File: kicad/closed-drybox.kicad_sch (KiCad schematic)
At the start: 25 parts, among them J1 Power_Jack, M1 Fan, M2 Fan, Q1 AO3400A, Q2 AO3400A, Q3 AO3400A, Q4 AO3400A, Q5 AO3400A, Q6 AO3400A, Q7 AO3400A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

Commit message: add anotations
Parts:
- gave numbers to parts that had none: 1
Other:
- moved on the sheet: JP1
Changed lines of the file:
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@@
 	(wire
 		(pts
-			(xy 120.65 46.99) (xy 124.46 46.99)
+			(xy 116.84 46.99) (xy 124.46 46.99)
 		)
 		(stroke
@@
 	(wire
 		(pts
-			(xy 113.03 46.99) (xy 55.88 46.99)
+			(xy 109.22 46.99) (xy 55.88 46.99)
 		)
 		(stroke
@@
 	(symbol
 		(lib_id "Jumper:SolderJumper_2_Open")
-		(at 116.84 46.99 0)
+		(at 113.03 46.99 0)
 		(unit 1)
 		(exclude_from_sim no)
@@
 		(dnp no)
 		(fields_autoplaced yes)
-		(property "Reference" "JP?"
-			(at 116.84 40.64 0)
+		(property "Reference" "JP1"
+			(at 113.03 40.64 0)
 			(effects
 				(font
@@
 		)
 		(property "Value" "SolderJumper_2_Open"
-			(at 116.84 43.18 0)
+			(at 113.03 43.18 0)
 			(effects
 				(font
@@
 		)
 		(property "Footprint" "Jumper:SolderJumper-2_P1.3mm_Open_RoundedPad1.0x1.5mm"
-			(at 116.84 46.99 0)
+			(at 113.03 46.99 0)
 			(effects
 				(font
@@
 		)
 		(property "Datasheet" "~"
-			(at 116.84 46.99 0)
+			(at 113.03 46.99 0)
 			(effects
 				(font
@@
 		)
 		(property "Description" "Solder Jumper, 2-pole, open"
-			(at 116.84 46.99 0)
+			(at 113.03 46.99 0)
 			(effects
 				(font
@@
 			(project ""
 				(path "/99399f2a-756c-4718-9b6a-bb37855e6538"
-					(reference "JP?")
+					(reference "JP1")
 					(unit 1)
 				)

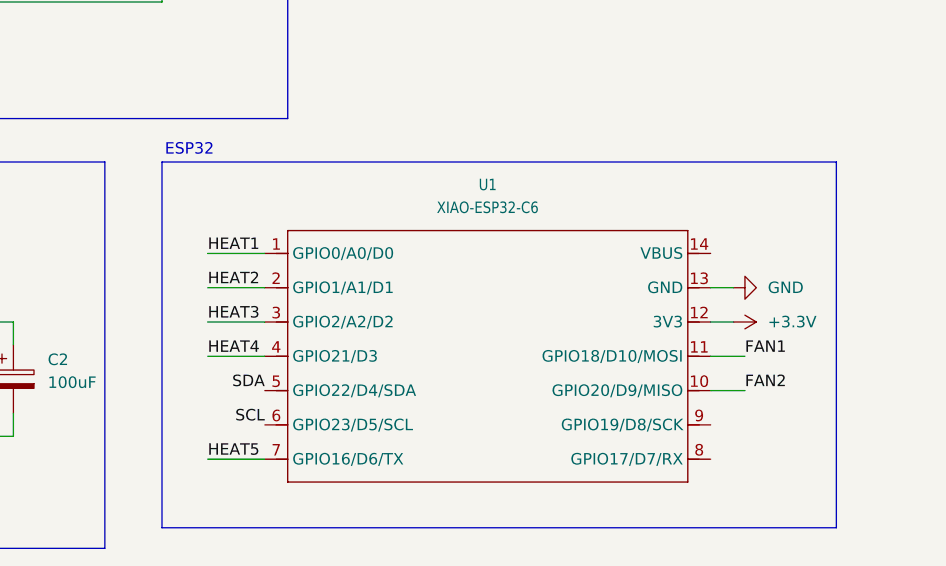
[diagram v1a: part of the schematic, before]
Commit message: fix labels
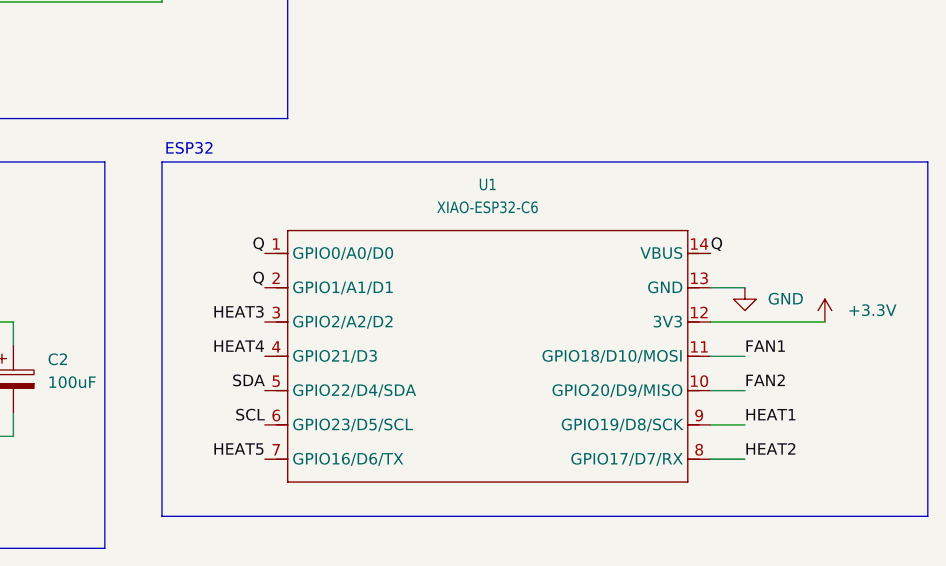
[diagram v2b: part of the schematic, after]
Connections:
- net HEAT1: now also U1.9 (GPIO19/D8/SCK); no longer U1.1 (GPIO0/A0/D0)
- net HEAT2: now also U1.8 (GPIO17/D7/RX); no longer U1.2 (GPIO1/A1/D1)
- net Q: now reaches U1.14 (VBUS)
- net Q: now also U1.1 (GPIO0/A0/D0), U1.2 (GPIO1/A1/D1)
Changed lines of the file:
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@@
 	(rectangle
 		(start 115.57 106.68)
-		(end 190.5 147.32)
+		(end 200.66 146.05)
 		(stroke
 			(width 0)
@@
 	(wire
 		(pts
-			(xy 176.53 120.65) (xy 179.07 120.65)
+			(xy 176.53 120.65) (xy 180.34 120.65)
 		)
 		(stroke
@@
 	(wire
 		(pts
-			(xy 120.65 116.84) (xy 127 116.84)
-		)
-		(stroke
-			(width 0)
-			(type default)
-		)
-	)
-	(wire
-		(pts
 			(xy 50.8 73.66) (xy 50.8 76.2)
 		)
@@
 	(wire
 		(pts
+			(xy 176.53 135.89) (xy 180.34 135.89)
+		)
+		(stroke
+			(width 0)
+			(type default)
+		)
+	)
+	(wire
+		(pts
 			(xy 109.22 46.99) (xy 55.88 46.99)
 		)
@@
 	(wire
 		(pts
-			(xy 176.53 124.46) (xy 179.07 124.46)
+			(xy 176.53 124.46) (xy 189.23 124.46)
 		)
 		(stroke
@@
 	(wire
 		(pts
-			(xy 120.65 120.65) (xy 127 120.65)
-		)
-		(stroke
-			(width 0)
-			(type default)
-		)
-	)
-	(wire
-		(pts
 			(xy 50.8 63.5) (xy 29.21 63.5)
 		)
@@
 	(wire
 		(pts
-			(xy 120.65 139.7) (xy 127 139.7)
-		)
-		(stroke
-			(width 0)
-			(type default)
-		)
-	)
-	(wire
-		(pts
 			(xy 72.39 86.36) (xy 72.39 88.9)
 		)
@@
 	(wire
 		(pts
-			(xy 120.65 124.46) (xy 127 124.46)
-		)
-		(stroke
-			(width 0)
-			(type default)
-		)
-	)
-	(wire
-		(pts
 			(xy 124.46 25.4) (xy 124.46 30.48)
 		)
@@
 	(wire
 		(pts
-			(xy 120.65 128.27) (xy 127 128.27)
-		)
-		(stroke
-			(width 0)
-			(type default)
-		)
-	)
-	(wire
-		(pts
 			(xy 176.53 34.29) (xy 176.53 27.94)
 		)
@@
 		(pts
 			(xy 99.06 124.46) (xy 83.82 124.46)
+		)
+		(stroke
+			(width 0)
+			(type default)
+		)
+	)
+	(wire
+		(pts
+			(xy 176.53 139.7) (xy 180.34 139.7)
 		)
 		(stroke
@@
 	)
 	(label "HEAT3"
-		(at 120.65 124.46 0)
+		(at 127 124.46 180)
+		(effects
+			(font
+				(size 1.27 1.27)
+			)
+			(justify right bottom)
+		)
+	)
+	(label "Q"
+		(at 176.53 116.84 0)
 		(effects
 			(font
@@
 		)
 	)
+	(label "Q"
+		(at 127 116.84 180)
+		(effects
+			(font
+				(size 1.27 1.27)
+			)
+			(justify right bottom)
+		)
+	)
 	(label "HEAT3"
 		(at 64.77 81.28 180)
@@
 		)
 	)
+	(label "Q"
+		(at 127 120.65 180)
+		(effects
+			(font
+				(size 1.27 1.27)
+			)
+			(justify right bottom)
+		)
+	)
 	(label "FAN1"
 		(at 143.51 55.88 180)
@@
 	)
 	(label "HEAT5"
-		(at 120.65 139.7 0)
+		(at 127 139.7 180)
 		(effects
 			(font
 				(size 1.27 1.27)
 			)
-			(justify left bottom)
+			(justify right bottom)
 		)
 	)
 	(label "HEAT1"
-		(at 120.65 116.84 0)
+		(at 180.34 135.89 0)
 		(effects
 			(font
@@
 	)
 	(label "HEAT2"
-		(at 120.65 120.65 0)
+		(at 180.34 139.7 0)
 		(effects
 			(font
@@
 	)
 	(label "HEAT4"
-		(at 120.65 128.27 0)
+		(at 127 128.27 180)
 		(effects
 			(font
 				(size 1.27 1.27)
 			)
-			(justify left bottom)
+			(justify right bottom)
 		)
 	)
@@
 	(symbol
 		(lib_id "power:+3.3V")
-		(at 179.07 124.46 270)
+		(at 189.23 124.46 0)
 		(unit 1)
 		(exclude_from_sim no)
@@
 		(fields_autoplaced yes)
 		(property "Reference" "#PWR08"
-			(at 175.26 124.46 0)
+			(at 189.23 128.27 0)
 			(effects
 				(font
@@
 		)
 		(property "Value" "+3.3V"
-			(at 182.88 124.4599 90)
+			(at 191.77 123.1899 0)
 			(effects
 				(font
@@
 		)
 		(property "Footprint" ""
-			(at 179.07 124.46 0)
+			(at 189.23 124.46 0)
 			(effects
 				(font
@@
 		)
 		(property "Datasheet" ""
-			(at 179.07 124.46 0)
+			(at 189.23 124.46 0)
 			(effects
 				(font
@@
 		)
 		(property "Description" "Power symbol creates a global label with name \"+3.3V\""
-			(at 179.07 124.46 0)
+			(at 189.23 124.46 0)
 			(effects
 				(font
@@
 	(symbol
 		(lib_id "power:GND")
-		(at 179.07 120.65 90)
+		(at 180.34 120.65 0)
 		(unit 1)
 		(exclude_from_sim no)
@@
 		(fields_autoplaced yes)
 		(property "Reference" "#PWR07"
-			(at 185.42 120.65 0)
+			(at 180.34 127 0)
 			(effects
 				(font
@@
 		)
 		(property "Value" "GND"
-			(at 182.88 120.6499 90)
-			(effects
-				(font
-					(size 1.27 1.27)
-				)
-				(justify right)
+			(at 182.88 121.9199 0)
+			(effects
+				(font
+					(size 1.27 1.27)
+				)
+				(justify left)
 			)
 		)
 		(property "Footprint" ""
-			(at 179.07 120.65 0)
+			(at 180.34 120.65 0)
 			(effects
 				(font
@@
 		)
 		(property "Datasheet" ""
-			(at 179.07 120.65 0)
+			(at 180.34 120.65 0)
 			(effects
 				(font
@@
 		)
 		(property "Description" "Power symbol creates a global label with name \"GND\" , ground"
-			(at 179.07 120.65 0)
-			(effects
-				(font
+			(at 180.34 120.65 0)
+			(effects
+				(font

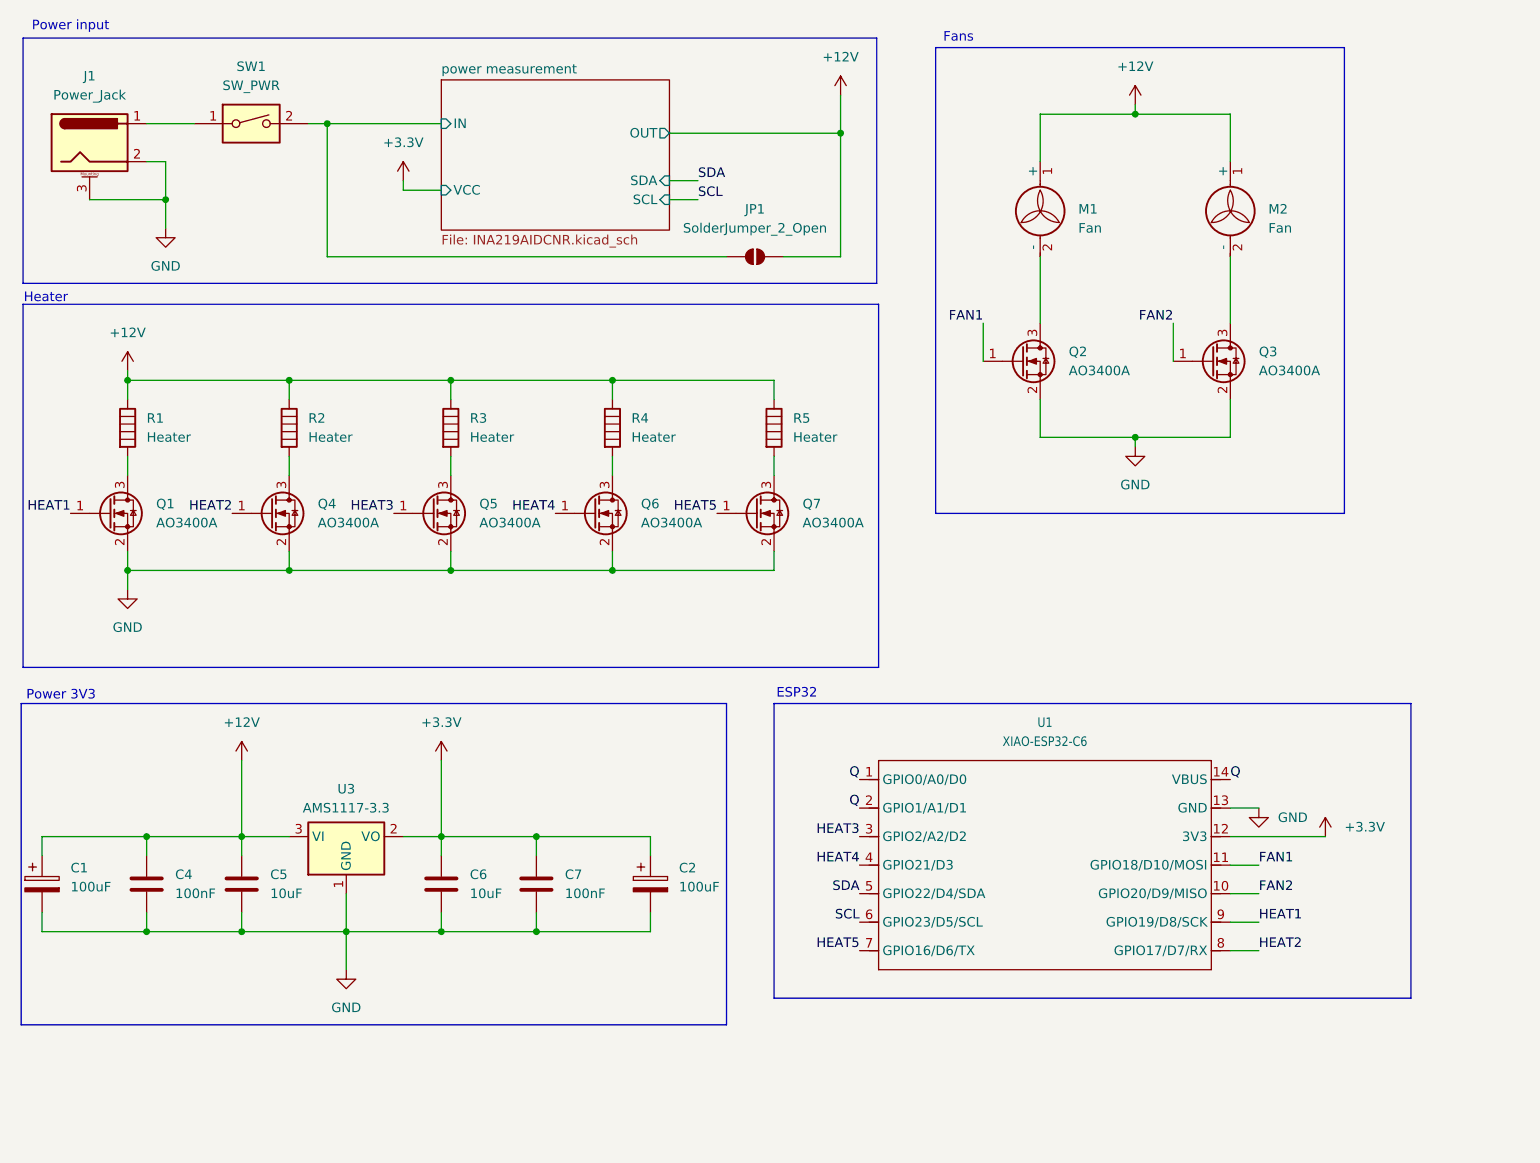
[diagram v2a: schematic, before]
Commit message: add diodes, fuse
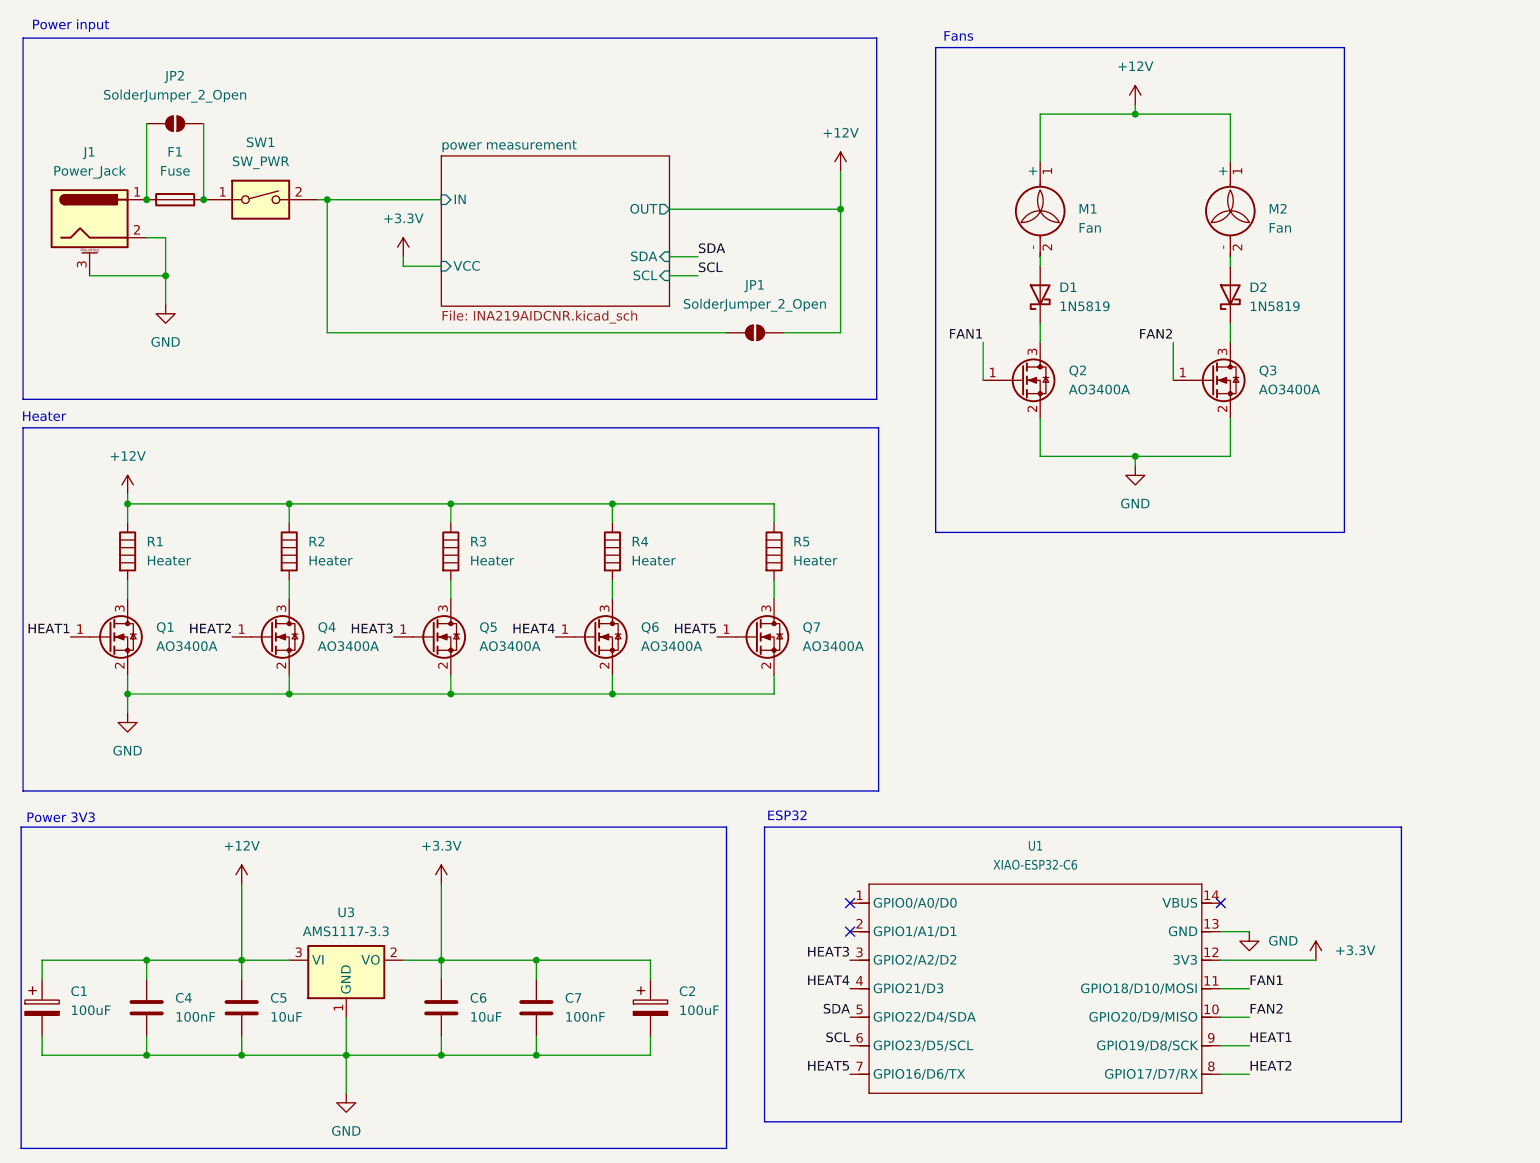
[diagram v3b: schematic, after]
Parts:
- added D1, D2: 1N5819, Diode_THT:D_DO-41_SOD81_P10.16mm_Horizontal, symbol Diode:1N5819
- added F1: Fuse, symbol Device:Fuse
- added JP2: SolderJumper_2_Open, Jumper:SolderJumper-2_P1.3mm_Open_RoundedPad1.0x1.5mm, symbol Jumper:SolderJumper_2_Open
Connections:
- net at Q2.3 (D): now also D1.1 (K); no longer M1.2 (-)
- net at Q3.3 (D): now also D2.1 (K); no longer M2.2 (-)
- net at J1.1: now also F1.1, JP2.1 (A); no longer SW1.1
- removed net Q: U1.1 (GPIO0/A0/D0), U1.14 (VBUS), U1.2 (GPIO1/A1/D1)
- new net: D1.2 (A), M1.2 (-)
- new net: F1.2, JP2.2 (B), SW1.1
- new net: D2.2 (A), M2.2 (-)
- no-connect marks 0 -> 3
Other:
- moved on the sheet: C1, C2, C4, C5, C6, C7, J1, JP1, Q1, Q2, Q3, Q4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

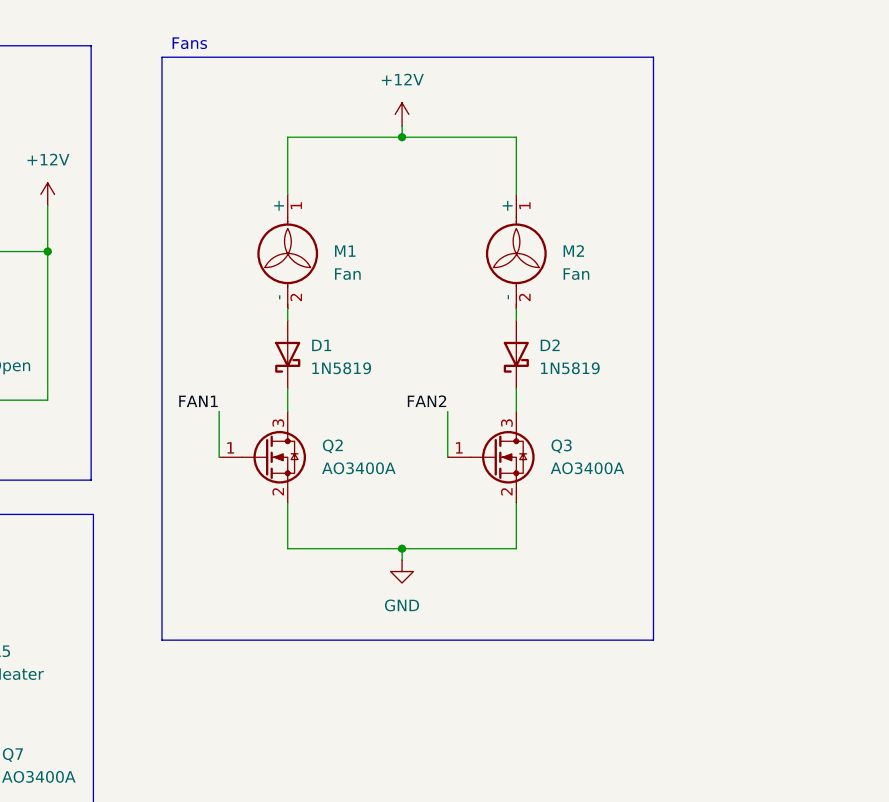
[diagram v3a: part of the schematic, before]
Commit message: fix flyback diodes
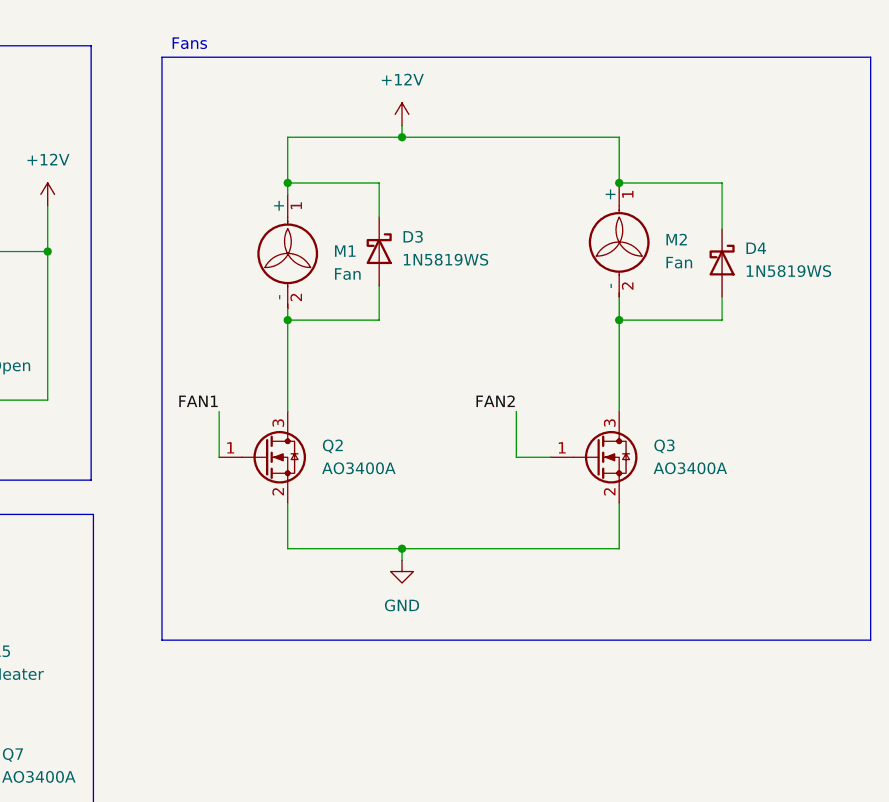
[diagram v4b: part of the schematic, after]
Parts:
- removed D1, D2: 1N5819, Diode_THT:D_DO-41_SOD81_P10.16mm_Horizontal, symbol Diode:1N5819
- added D3, D4: 1N5819WS, Diode_SMD:D_SOD-323, symbol Diode:1N5819WS
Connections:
- net +12V: now also D3.1 (K), D4.1 (K)
- net at Q2.3 (D): now also M1.2 (-), D3.2 (A)
- net at Q3.3 (D): now also M2.2 (-), D4.2 (A)
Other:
- moved on the sheet: M2, Q3

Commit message: add part #'s
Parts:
- D3, D4: LCSC (none) -> C191023
- J1: LCSC (none) -> C720558
- R1, R2, R3, R4, R5: LCSC (none) -> C158012
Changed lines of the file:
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@@
+			)
+		)
+		(property "LCSC" "C158012"
+			(at 74.93 85.0899 0)
+			(effects
+				(font
+					(size 1.27 1.27)
+				)
+				(hide yes)
 			)
 		)
@@
 			)
 		)
+		(property "LCSC" "C191023"
+			(at 201.93 40.3224 0)
+			(effects
+				(font
+					(size 1.27 1.27)
+				)
+				(hide yes)
+			)
+		)
 		(pin "1"
 		)
@@
 			)
 		)
+		(property "LCSC" "C720558"
+			(at 24.13 33.02 0)
+			(effects
+				(font
+					(size 1.27 1.27)
+				)
+				(hide yes)
+			)
+		)
 		(pin "2"
 		)
@@
 			)
 		)
+		(property "LCSC" "C158012"
+			(at 53.34 85.0899 0)
+			(effects
+				(font
+					(size 1.27 1.27)
+				)
+				(hide yes)
+			)
+		)
 		(pin "2"
 		)
@@
 			)
 		)
+		(property "LCSC" "C158012"
+			(at 118.11 85.0899 0)
+			(effects
+				(font
+					(size 1.27 1.27)
+				)
+				(hide yes)
+			)
+		)
 		(pin "2"
 		)
@@
 			)
 		)
+		(property "LCSC" "C158012"
+			(at 31.75 85.0899 0)
+			(effects
+				(font
+					(size 1.27 1.27)
+				)
+				(hide yes)
+			)
+		)
 		(pin "2"
 		)
@@
 			)
 		)
+		(property "LCSC" "C191023"
+			(at 163.83 39.0524 0)
+			(effects
+				(font
+					(size 1.27 1.27)
+				)
+				(hide yes)
+			)
+		)
 		(pin "2"
 		)
@@
 			(effects
 				(font
+					(size 1.27 1.27)
+				)
+				(hide yes)
+			)
+		)
+		(property "LCSC" "C158012"
+			(at 96.52 85.0899 0)
+			(effects
+				(font
